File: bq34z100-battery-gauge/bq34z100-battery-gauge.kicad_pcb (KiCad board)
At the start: 4 copper layers, 73.3 x 68.9 mm, 52 parts, among them J1 Conn_01x04, J11 LED, J2 ALERT, J3 NTC, J4 LED_DISP, J5 BAT, J6 BAT, J7 LOAD, J8 LOAD, Q2 2N7002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

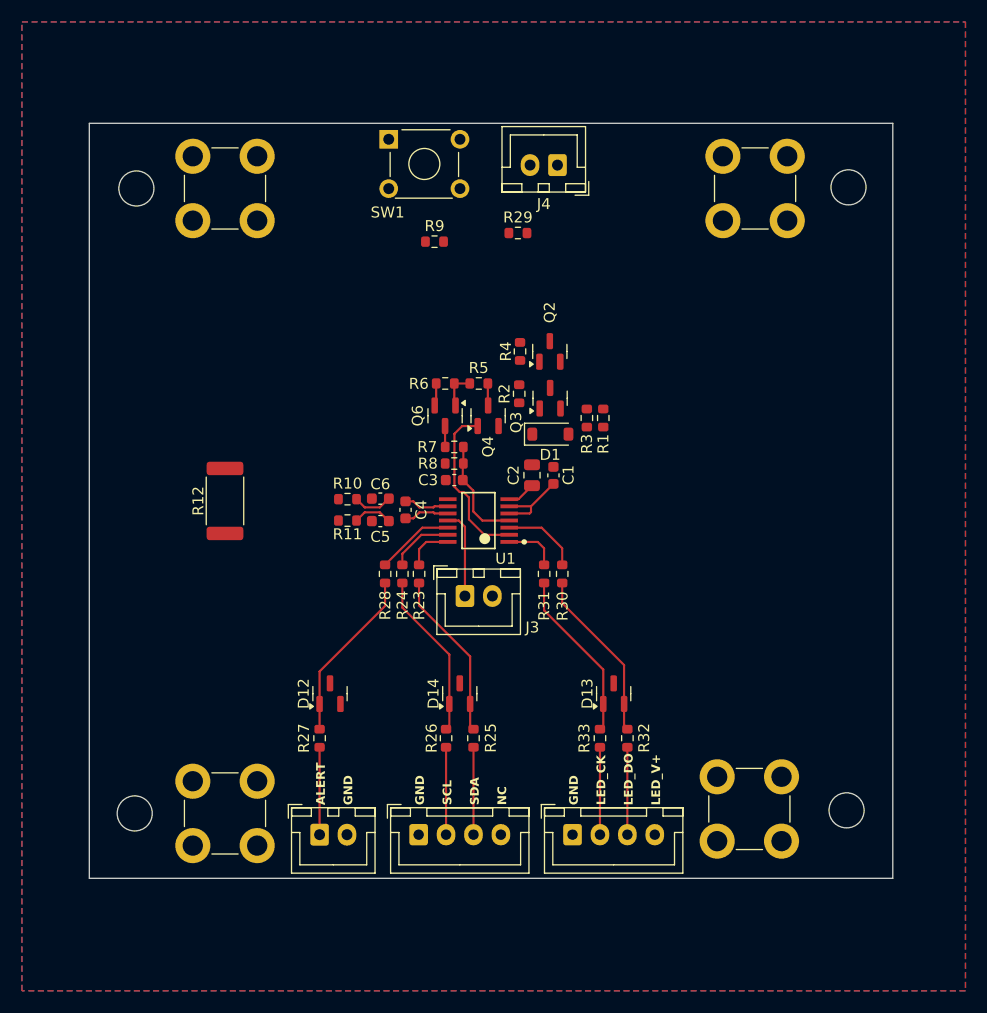
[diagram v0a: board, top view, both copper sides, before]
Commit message: Change Resistor to issabelenhurt, change mounting hole dimension
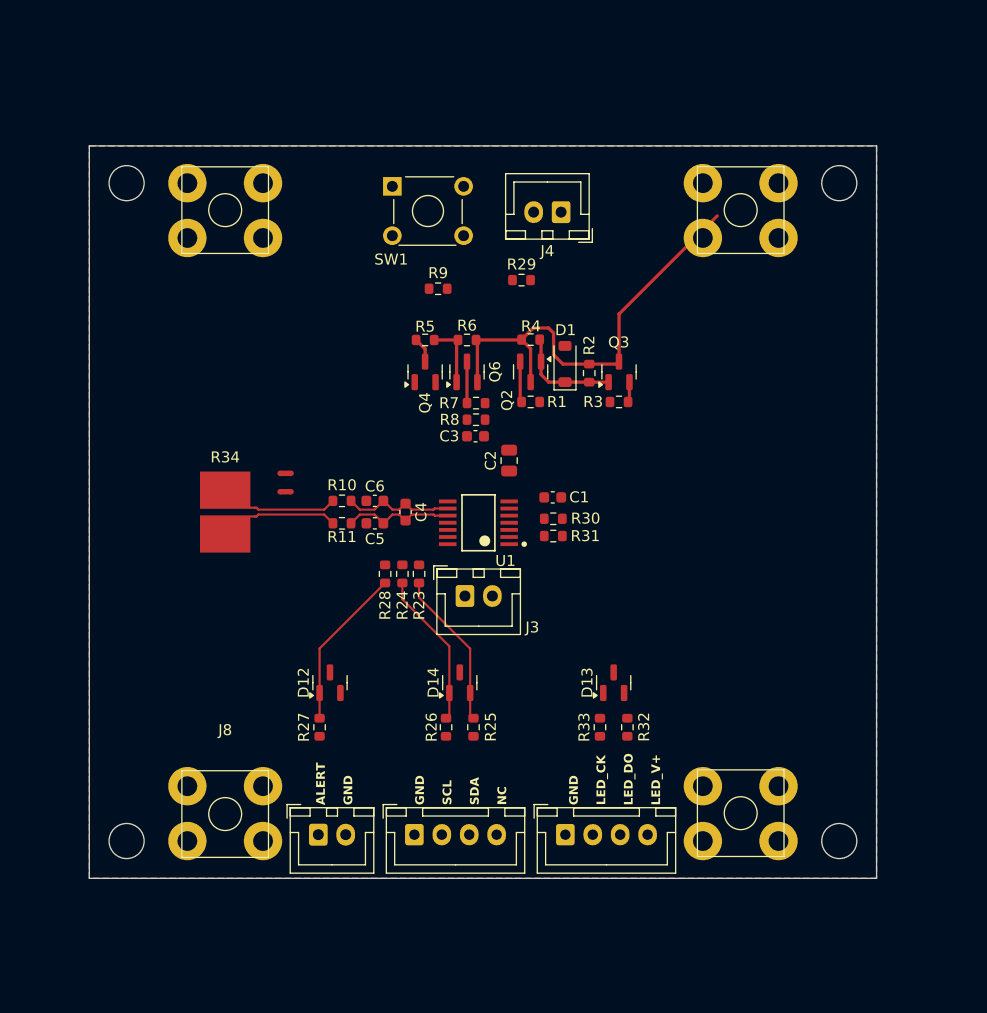
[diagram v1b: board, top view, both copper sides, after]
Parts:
- removed R12: .010R 75ppm, Resistor_SMD:R_2512_6332Metric
- added NT2: NetTie_2, NetTie:NetTie-2_SMD_Pad0.5mm, F.Cu at (112.9, 100.1)
- added NT3: NetTie_2, NetTie:NetTie-2_SMD_Pad0.5mm, F.Cu at (112.9, 98.4)
- added R34: 0.01, shunt-resistor:Isabellenhuette-SMT-R010-1.0, F.Cu at (107.4, 101.9)
- J5, J6, J7, J8: footprint TerminalBlock_Wuerth:Wuerth_REDCUBE-THR_WP-THRBU_74650174_THR -> Plugin_terminal:square_terminal
- moved Q4 7.00 mm to (125.7, 89.1)
- moved R1 6.79 mm to (135.3, 91.9), turned to 180 degrees
- moved Q3 6.73 mm to (143.4, 89.1)
- moved R2 6.66 mm to (140.6, 89.3)
- moved D1 6.53 mm to (138.4, 88.4), turned to 90 degrees
- moved R5 6.30 mm to (125.7, 86.2), turned to 0 degrees
- moved R30 5.10 mm to (137.4, 102.5), turned to 180 degrees
- moved Q6 4.47 mm to (129.5, 89.1), turned to 90 degrees
- moved R7 4.47 mm to (130.3, 92.0)
- moved R8 4.47 mm to (130.3, 93.5)
- moved C3 4.44 mm to (130.3, 95.0)
- moved R6 4.44 mm to (129.5, 86.2), turned to 0 degrees
- moved SW1 4.31 mm to (122.7, 72.2)
- moved R9 4.31 mm to (126.9, 81.6)
- moved J4 4.31 mm to (138.1, 74.6)
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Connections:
- C1 pad 2: GND -> GNDA
- C2 pad 2: GND -> GNDA
- C3 pad 2: GND -> GNDA
- R10 pad 1: VBAT- -> /SENSE_P
- R11 pad 1: PACK- -> /SENSE_N
- R8 pad 1: GND -> GNDA
- U1 pad 8: GND -> GNDA
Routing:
- net VBAT+: track 2.06 -> 41.2 mm
- net Net-(D13-K-Pad2): track 15.8 -> 0.00 mm
- net Net-(D13-K-Pad1): track 15.7 -> 0.00 mm
- net /VEN: track 15.2 -> 0.00 mm
- net Net-(U1-BAT): track 9.91 -> 0.00 mm
- net Net-(D1-K): track 0.00 -> 9.69 mm
- net Net-(J3-Pin_1): track 8.12 -> 0.00 mm
- net Net-(J2-Pin_1): track 7.97 -> 0.00 mm
- net Net-(J11-Pin_3): track 7.97 -> 0.00 mm
- net Net-(J11-Pin_2): track 7.97 -> 0.00 mm
- net Net-(J1-Pin_3): track 7.97 -> 0.00 mm
- net Net-(J1-Pin_2): track 7.97 -> 0.00 mm
- net /SENSE_P: track 0.00 -> 7.53 mm
- net /SENSE_N: track 0.00 -> 7.53 mm
- net REGIN: track 7.46 -> 0.00 mm
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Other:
- board size 73.3 x 68.9 mm -> 71.8 x 66.8 mm

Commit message: 1. Finished tracks, (need to verify grounding layer below battery tracks). 2. Added more literature document
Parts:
- removed R29: 1K, Resistor_SMD:R_0603_1608Metric
- added TP1: TestPoint, TestPoint:TestPoint_Pad_D1.0mm, F.Cu at (102.0, 100.9)
- added TP2: TestPoint, TestPoint:TestPoint_Pad_D1.0mm, F.Cu at (102.0, 102.9)
- moved R9 10.4 mm to (131.4, 72.2), turned to 90 degrees
- moved SW1 6.88 mm to (129.2, 74.5), turned to 180 degrees
- moved C1 2.84 mm to (135.6, 98.3), turned to 90 degrees
- moved J4 2.32 mm to (138.1, 72.3)
- moved NT3 1.37 mm to (112.9, 99.8)
- moved R30 1.02 mm to (137.4, 103.6)
- moved NT2 1.02 mm to (112.9, 101.1)
- moved R31 0.94 mm to (137.4, 105.1)
- moved C2 0.91 mm to (133.3, 98.1)
- moved D13 0.66 mm to (142.2, 117.5)
- moved R32 0.66 mm to (143.5, 121.6)
- moved R33 0.66 mm to (141.0, 121.6)
- moved D14 0.39 mm to (128.4, 117.5)
- moved R25 0.39 mm to (129.7, 121.6)
- moved R26 0.39 mm to (127.2, 121.6)
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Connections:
- J4 pad 1: Net-(J4-Pin_1) -> /VEN
- J4 pad 2: /VEN -> /LED_SW
- R9 pad 2: Net-(R9-Pad2) -> /LED_SW
- SW1 pad 2: Net-(R9-Pad2) -> /LED_SW
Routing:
- net /VEN: track 0.00 -> 55.2 mm
- net /REG25: track 0.00 -> 44.8 mm, vias 0 -> 2
- net GNDA: track 0.00 -> 42.2 mm, vias 0 -> 7
- net REGIN: track 0.00 -> 25.6 mm
- net Net-(D13-K-Pad2): track 0.00 -> 19.4 mm
- net Net-(D13-K-Pad1): track 0.00 -> 17.1 mm
- net /LED_SW: track 0.00 -> 13.9 mm
- net Net-(U1-BAT): track 0.00 -> 12.9 mm
- net Net-(J2-Pin_1): track 0.00 -> 8.97 mm
- net Net-(J11-Pin_3): track 0.00 -> 8.97 mm
- net Net-(J11-Pin_2): track 0.00 -> 8.97 mm
- net Net-(J1-Pin_3): track 0.00 -> 8.97 mm
- net Net-(J1-Pin_2): track 0.00 -> 8.97 mm
- net Net-(J3-Pin_1): track 0.00 -> 7.90 mm
- net Net-(U1-P5/HDQ): track 0.00 -> 7.04 mm
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- added copper zone on B.Cu, net PACK-
- added copper zone on F.Cu, net PACK-
- added copper zone on B.Cu, net VBAT+
- added copper zone on F.Cu, net VBAT+
- added copper zone on B.Cu, net VBAT-
- added copper zone on F.Cu, net VBAT-
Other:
- board text added: "SENSE_N"
- board text added: "SENSE_P"
